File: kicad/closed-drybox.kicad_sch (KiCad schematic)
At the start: 29 parts, among them J1 Power_Jack, M1 Fan, M2 Fan, Q1 AO3400A, Q2 AO3400A, Q3 AO3400A, Q4 AO3400A, Q5 AO3400A, Q6 AO3400A, Q7 AO3400A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

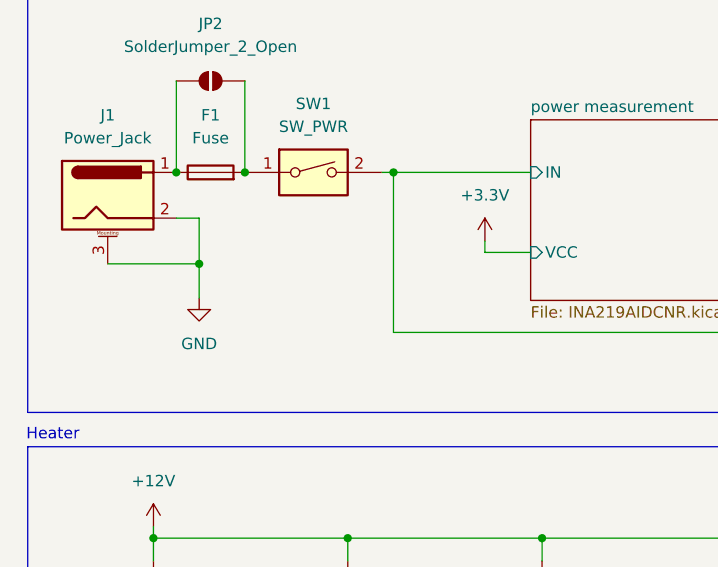
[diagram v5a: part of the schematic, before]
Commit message: add jumper for power
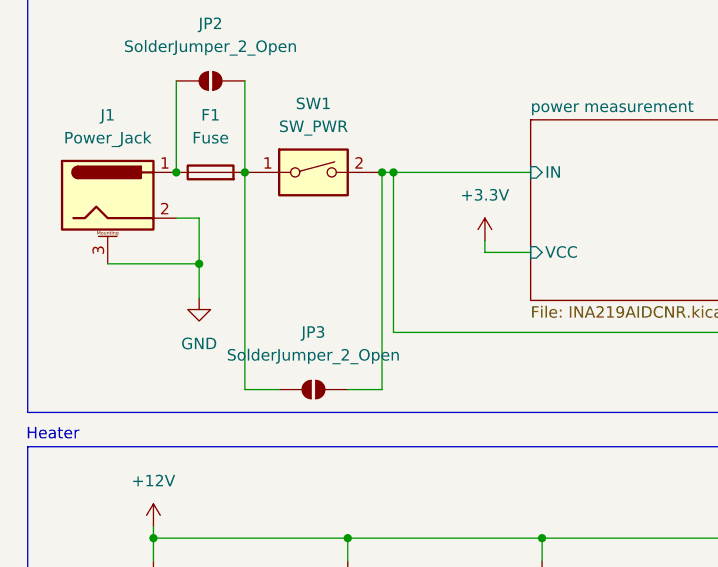
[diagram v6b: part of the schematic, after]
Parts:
- added JP3: SolderJumper_2_Open, Jumper:SolderJumper-2_P1.3mm_Open_RoundedPad1.0x1.5mm, symbol Jumper:SolderJumper_2_Open
- SW1: symbol CustomSymbols:SW_PWR -> CustomLibary:SW_PWR
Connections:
- net power measurement/IN: now also JP3.2 (B)
- net at F1.2, JP2.2 (B), SW1.1: now also JP3.1 (A)
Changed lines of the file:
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@@
 	)
 	(junction
+		(at 54.61 39.37)
+		(diameter 0)
+		(color 0 0 0 0)
+	)
+	(junction
 		(at 151.13 33.02)
 		(diameter 0)
@@
 	(wire
 		(pts
+			(xy 54.61 63.5) (xy 54.61 39.37)
+		)
+		(stroke
+			(width 0)
+			(type default)
+		)
+	)
+	(wire
+		(pts
 			(xy 71.12 151.13) (xy 71.12 153.67)
 		)
@@
 	(wire
 		(pts
+			(xy 39.37 63.5) (xy 39.37 39.37)
+		)
+		(stroke
+			(width 0)
+			(type default)
+		)
+	)
+	(wire
+		(pts
 			(xy 34.29 44.45) (xy 34.29 49.53)
 		)
@@
 	(wire
 		(pts
+			(xy 50.8 63.5) (xy 54.61 63.5)
+		)
+		(stroke
+			(width 0)
+			(type default)
+		)
+	)
+	(wire
+		(pts
 			(xy 29.21 102.87) (xy 29.21 105.41)
 		)
@@
 	(wire
 		(pts
+			(xy 43.18 63.5) (xy 39.37 63.5)
+		)
+		(stroke
+			(width 0)
+			(type default)
+		)
+	)
+	(wire
+		(pts
 			(xy 44.45 130.81) (xy 44.45 140.97)
 		)
@@
 	)
 	(symbol
+		(lib_id "Jumper:SolderJumper_2_Open")
+		(at 46.99 63.5 0)
+		(unit 1)
+		(exclude_from_sim no)
+		(in_bom no)
+		(on_board yes)
+		(dnp no)
+		(fields_autoplaced yes)
+		(property "Reference" "JP3"
+			(at 46.99 57.15 0)
+			(effects
+				(font
+					(size 1.27 1.27)
+				)
+			)
+		)
+		(property "Value" "SolderJumper_2_Open"
+			(at 46.99 59.69 0)
+			(effects
+				(font
+					(size 1.27 1.27)
+				)
+			)
+		)
+		(property "Footprint" "Jumper:SolderJumper-2_P1.3mm_Open_RoundedPad1.0x1.5mm"
+			(at 46.99 63.5 0)
+			(effects
+				(font
+					(size 1.27 1.27)
+				)
+				(hide yes)
+			)
+		)
+		(property "Datasheet" "~"
+			(at 46.99 63.5 0)
+			(effects
+				(font
+					(size 1.27 1.27)
+				)
+				(hide yes)
+			)
+		)
+		(property "Description" "Solder Jumper, 2-pole, open"
+			(at 46.99 63.5 0)
+			(effects
+				(font
+					(size 1.27 1.27)
+				)
+				(hide yes)
+			)
+		)
+		(pin "1"
+		)
+		(pin "2"
+		)
+		(instances
+			(project "closed-drybox"
+				(path "/99399f2a-756c-4718-9b6a-bb37855e6538"
+					(reference "JP3")
+					(unit 1)
+				)
+			)
+		)
+	)
+	(symbol
 		(lib_id "power:+12V")
 		(at 163.83 26.67 0)
@@
 	)
 	(symbol
-		(lib_id "CustomSymbols:SW_PWR")
+		(lib_id "CustomLibary:SW_PWR")
 		(at 46.99 39.37 0)
 		(unit 1)

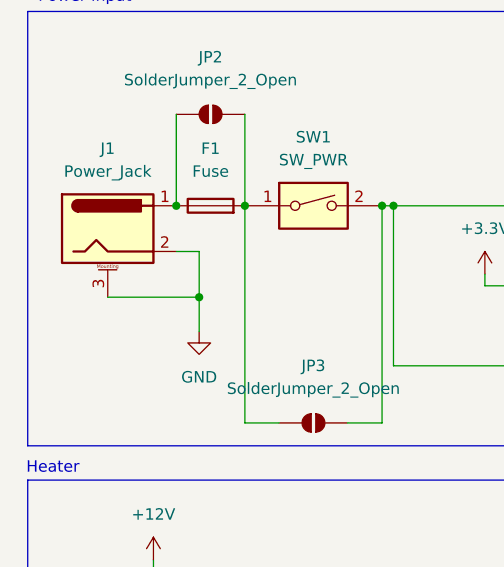
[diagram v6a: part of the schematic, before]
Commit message: add power jack symbol
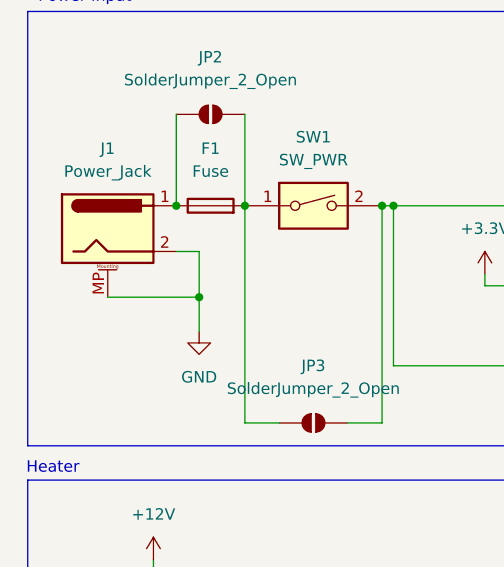
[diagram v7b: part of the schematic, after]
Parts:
- removed J1: Power_Jack, Connector_BarrelJack:BarrelJack_Horizontal, symbol CustomSymbols:Power_Jack
- added J1: Power_Jack, Connector_BarrelJack:BarrelJack_Horizontal, symbol CustomLibary:Power_Jack
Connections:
- net GND: now also J1.2, J1.MP (MountPin)
- net at F1.1, JP2.1 (A): now also J1.1
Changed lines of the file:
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@@
+	)
+	(junction
+		(at 58.42 153.67)
+		(diameter 0)
+		(color 0 0 0 0)
+	)
+	(junction
+		(at 44.45 140.97)
+		(diameter 0)
+		(color 0 0 0 0)
+	)
+	(junction
+		(at 93.98 105.41)
+		(diameter 0)
+		(color 0 0 0 0)
+	)
+	(junction
+		(at 71.12 140.97)
+		(diameter 0)
+		(color 0 0 0 0)
+	)
+	(junction
+		(at 39.37 39.37)
+		(diameter 0)
+		(color 0 0 0 0)
+	)
+	(junction
+		(at 72.39 105.41)
+		(diameter 0)
+		(color 0 0 0 0)
+	)
+	(junction
+		(at 187.96 33.02)
+		(diameter 0)
+		(color 0 0 0 0)
+	)
+	(junction
+		(at 93.98 80.01)
+		(diameter 0)
+		(color 0 0 0 0)
+	)
+	(junction
+		(at 187.96 48.26)
+		(diameter 0)
+		(color 0 0 0 0)
+	)
+	(junction
+		(at 29.21 105.41)
+		(diameter 0)
+		(color 0 0 0 0)
+	)
+	(junction
+		(at 55.88 39.37)
+		(diameter 0)
+		(color 0 0 0 0)
+	)
+	(junction
+		(at 54.61 39.37)
+		(diameter 0)
+		(color 0 0 0 0)
+	)
+	(junction
+		(at 151.13 33.02)
+		(diameter 0)
+		(color 0 0 0 0)
+	)
+	(junction
+		(at 50.8 80.01)
+		(diameter 0)
+		(color 0 0 0 0)
+	)
+	(junction
+		(at 50.8 105.41)
+		(diameter 0)
+		(color 0 0 0 0)
+	)
+	(junction
+		(at 124.46 40.64)
+		(diameter 0)
+		(color 0 0 0 0)
+	)
+	(junction
+		(at 163.83 73.66)
+		(diameter 0)
+		(color 0 0 0 0)
+	)
+	(junction
+		(at 163.83 27.94)
+		(diameter 0)
+		(color 0 0 0 0)
 	)
 	(junction
 		(at 31.75 39.37)
-		(diameter 0)
-		(color 0 0 0 0)
-	)
-	(junction
-		(at 58.42 153.67)
-		(diameter 0)
-		(color 0 0 0 0)
-	)
-	(junction
-		(at 44.45 140.97)
-		(diameter 0)
-		(color 0 0 0 0)
-	)
-	(junction
-		(at 93.98 105.41)
-		(diameter 0)
-		(color 0 0 0 0)
-	)
-	(junction
-		(at 71.12 140.97)
-		(diameter 0)
-		(color 0 0 0 0)
-	)
-	(junction
-		(at 39.37 39.37)
-		(diameter 0)
-		(color 0 0 0 0)
-	)
-	(junction
-		(at 72.39 105.41)
-		(diameter 0)
-		(color 0 0 0 0)
-	)
-	(junction
-		(at 187.96 33.02)
-		(diameter 0)
-		(color 0 0 0 0)
-	)
-	(junction
-		(at 93.98 80.01)
-		(diameter 0)
-		(color 0 0 0 0)
-	)
-	(junction
-		(at 187.96 48.26)
-		(diameter 0)
-		(color 0 0 0 0)
-	)
-	(junction
-		(at 29.21 105.41)
-		(diameter 0)
-		(color 0 0 0 0)
-	)
-	(junction
-		(at 55.88 39.37)
-		(diameter 0)
-		(color 0 0 0 0)
-	)
-	(junction
-		(at 54.61 39.37)
-		(diameter 0)
-		(color 0 0 0 0)
-	)
-	(junction
-		(at 151.13 33.02)
-		(diameter 0)
-		(color 0 0 0 0)
-	)
-	(junction
-		(at 50.8 80.01)
-		(diameter 0)
-		(color 0 0 0 0)
-	)
-	(junction
-		(at 50.8 105.41)
-		(diameter 0)
-		(color 0 0 0 0)
-	)
-	(junction
-		(at 124.46 40.64)
-		(diameter 0)
-		(color 0 0 0 0)
-	)
-	(junction
-		(at 163.83 73.66)
-		(diameter 0)
-		(color 0 0 0 0)
-	)
-	(junction
-		(at 163.83 27.94)
 		(diameter 0)
 		(color 0 0 0 0)
@@
 	)
 	(symbol
+		(lib_id "CustomLibary:Power_Jack")
+		(at 24.13 41.91 0)
+		(unit 1)
+		(exclude_from_sim no)
+		(in_bom yes)
+		(on_board yes)
+		(dnp no)
+		(fields_autoplaced yes)
+		(property "Reference" "J1"
+			(at 24.13 33.02 0)
+			(effects
+				(font
+					(size 1.27 1.27)
+				)
+			)
+		)
+		(property "Value" "Power_Jack"
+			(at 24.13 35.56 0)
+			(effects
+				(font
+					(size 1.27 1.27)
+				)
+			)
+		)
+		(property "Footprint" "Connector_BarrelJack:BarrelJack_Horizontal"
+			(at 25.4 42.926 0)
+			(effects
+				(font
+					(size 1.27 1.27)
+				)
+				(hide yes)
+			)
+		)
+		(property "Datasheet" "~"
+			(at 25.4 42.926 0)
+			(effects
+				(font
+					(size 1.27 1.27)
+				)
+				(hide yes)
+			)
+		)
+		(property "Description" "DC Barrel Jack with a mounting pin"
+			(at 24.13 41.91 0)
+			(effects
+				(font
+					(size 1.27 1.27)
+				)
+				(hide yes)
+			)
+		)
+		(property "LCSC" "C720558"
+			(at 24.13 33.02 0)
+			(effects
+				(font
+					(size 1.27 1.27)
+				)
+				(hide yes)
+			)
+		)
+		(pin "MP"
+		)
+		(pin "1"
+		)
+		(pin "2"
+		)
+		(instances
+			(project ""
+				(path "/99399f2a-756c-4718-9b6a-bb37855e6538"
+					(reference "J1")
+					(unit 1)
+				)
+			)
+		)
+	)
+	(symbol
 		(lib_id "Diode:1N5819WS")
 		(at 199.39 41.91 270)
@@
 					(unit 1)
 				)
-			)
-		)
-	)
-	(symbol
-		(lib_id "CustomSymbols:Power_Jack")
-		(at 24.13 41.91 0)
-		(unit 1)
-		(exclude_from_sim no)
-		(in_bom yes)
-		(on_board yes)
-		(dnp no)
-		(fields_autoplaced yes)
-		(property "Reference" "J1"
-			(at 24.13 33.02 0)
-			(effects
-				(font
-					(size 1.27 1.27)
-				)
-			)
-		)
-		(property "Value" "Power_Jack"
-			(at 24.13 35.56 0)
-			(effects
-				(font
-					(size 1.27 1.27)
-				)
-			)
-		)
-		(property "Footprint" "Connector_BarrelJack:BarrelJack_Horizontal"
-			(at 25.4 42.926 0)
-			(effects
-				(font
-					(size 1.27 1.27)
-				)
-				(hide yes)
-			)
-		)
-		(property "Datasheet" "~"
-			(at 25.4 42.926 0)
-			(effects
-				(font
-					(size 1.27 1.27)
-				)
-				(hide yes)
-			)
-		)
-		(property "Description" "Power_Jack"
-			(at 24.13 41.91 0)
-			(effects
-				(font
-					(size 1.27 1.27)
-				)
-				(hide yes)
-			)
-		)
-		(property "LCSC" "C720558"
-			(at 24.13 33.02 0)
-			(effects
-				(font
-					(size 1.27 1.27)
-				)
-				(hide yes)
-			)
-		)
-		(pin "2"
-		)
-		(pin "1"
-		)
-		(pin "3"
-		)
-		(instances
-			(project "closed-drybox"
-				(path "/99399f2a-756c-4718-9b6a-bb37855e6538"
-					(reference "J1")
-					(unit 1)
-				)
